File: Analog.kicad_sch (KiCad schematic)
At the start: 0 parts

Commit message: working on audio dac
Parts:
- added U3: MAX98357A, Package_DFN_QFN:TQFN-16-1EP_3x3mm_P0.5mm_EP1.23x1.23mm, symbol Audio:MAX98357A
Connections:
- new net +3V3: U3.7 (VDD), U3.8 (VDD)
- new net GND: U3.11 (GND), U3.15 (GND), U3.17 (PAD), U3.3 (GND)
- new net I2S3_CK: U3.16 (BCLK)
- new net I2S3_SD: U3.1 (DIN)
- new net I2S3_WS: U3.14 (LRCLK)

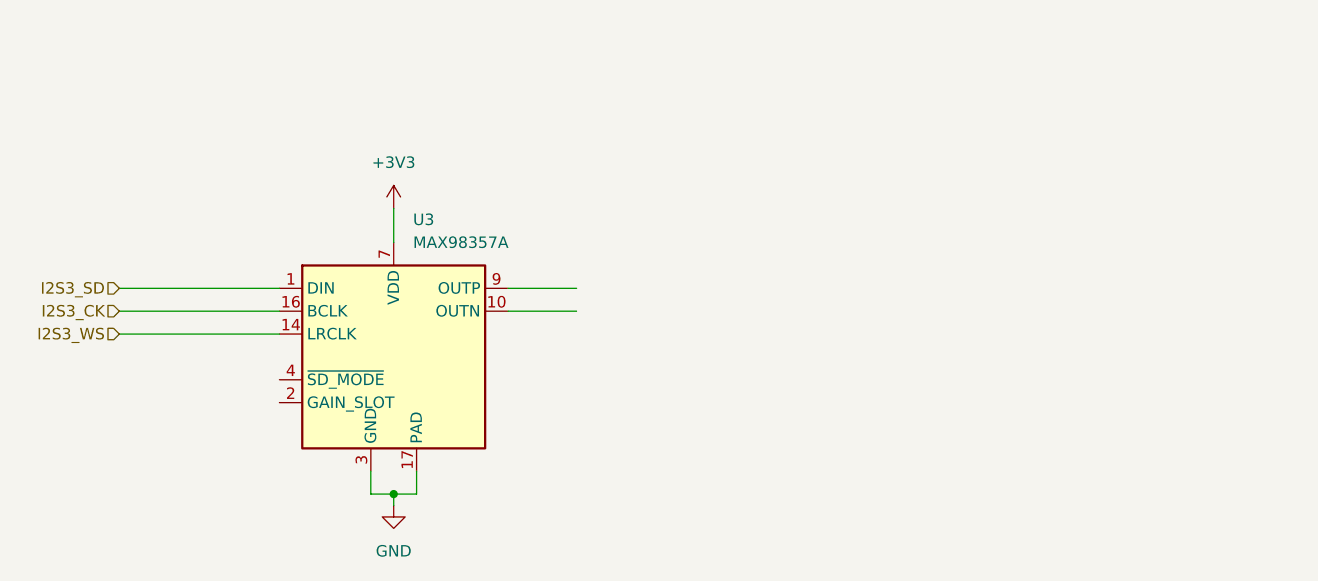
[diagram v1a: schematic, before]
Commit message: audio  dac added
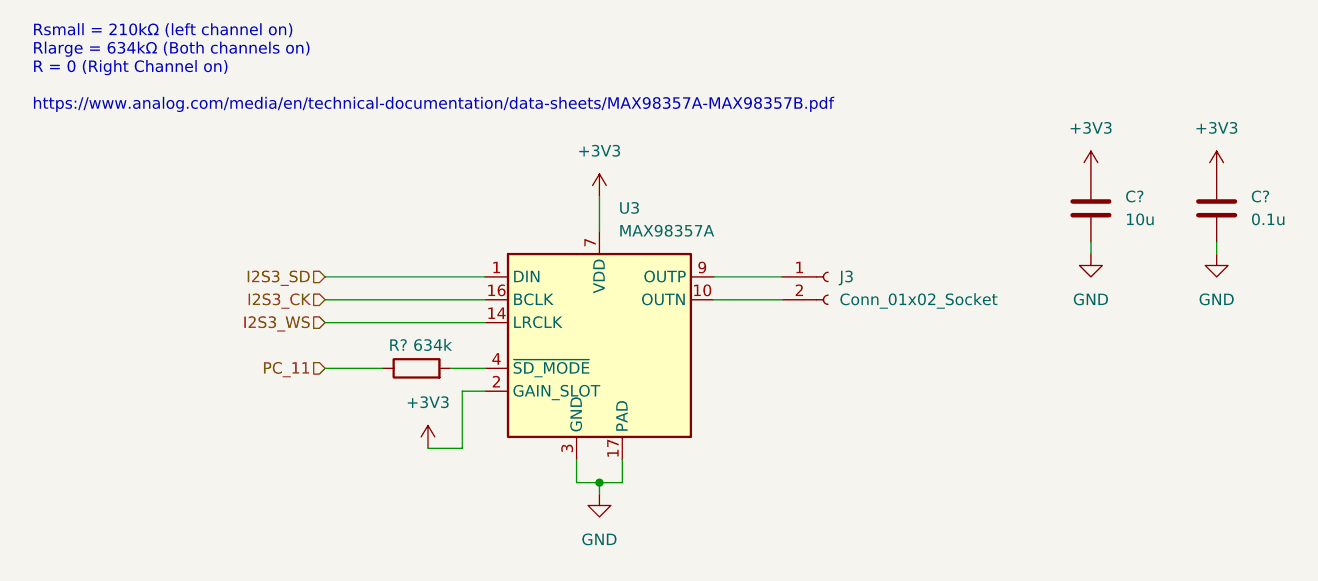
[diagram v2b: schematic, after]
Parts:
- added C?: 0.1u, Capacitor_SMD:C_0603_1608Metric, symbol Device:C
- added C?: 10u, Capacitor_SMD:C_0603_1608Metric, symbol Device:C
- added J3: Conn_01x02_Socket, symbol Connector:Conn_01x02_Socket
- added R?: 634k, Package_DFN_QFN:TQFN-16-1EP_3x3mm_P0.5mm_EP1.23x1.23mm, symbol Device:R
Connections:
- net +3V3: now also U3.2 (GAIN_SLOT), C?.1, C?.1
- net GND: now also C?.2, C?.2
- net at U3.10 (OUTN): now also J3.2 (Pin_2)
- net at U3.4 (~{SD_MODE}): now also R?.2
- net at U3.9 (OUTP): now also J3.1 (Pin_1)
- new net PC_11: R?.1
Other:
- note added: "Rsmall = 210kΩ (left channel on) Rlarge = 634kΩ (Both channels on) R = 0 (Right Channel on) https://www.analog.com/media/en/technical-documentation/data-sheets/MAX98357A-MAX98357B.pdf"
- moved on the sheet: U3

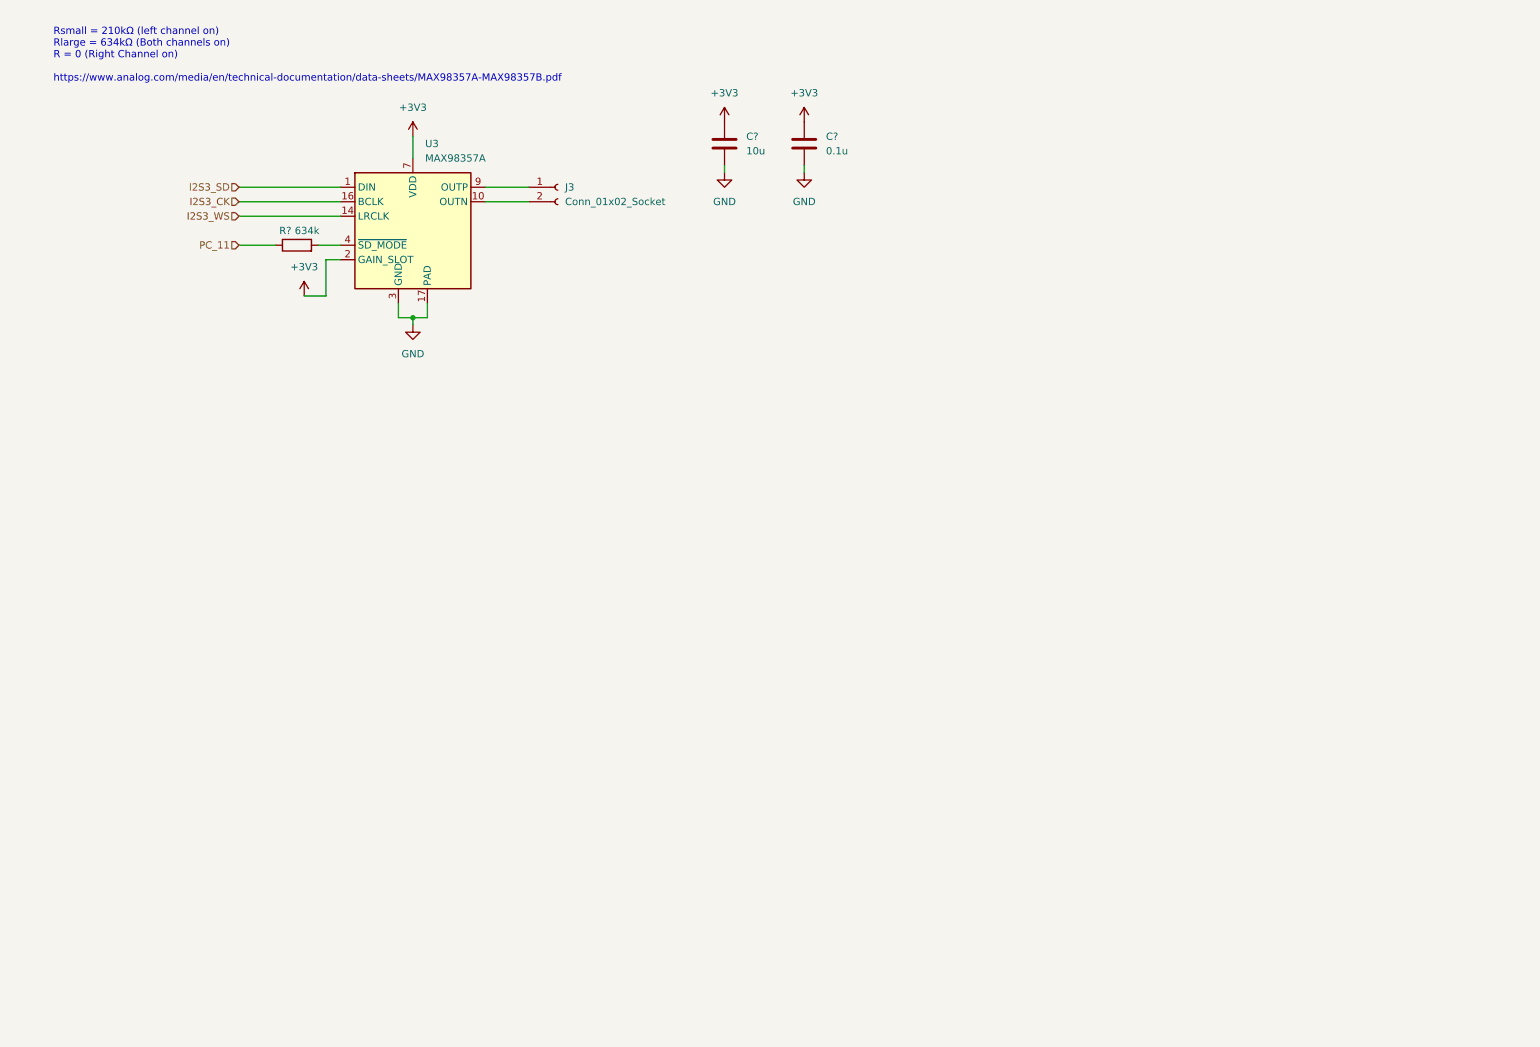
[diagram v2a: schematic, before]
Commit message: fixing audio dac, moving audio to analog section
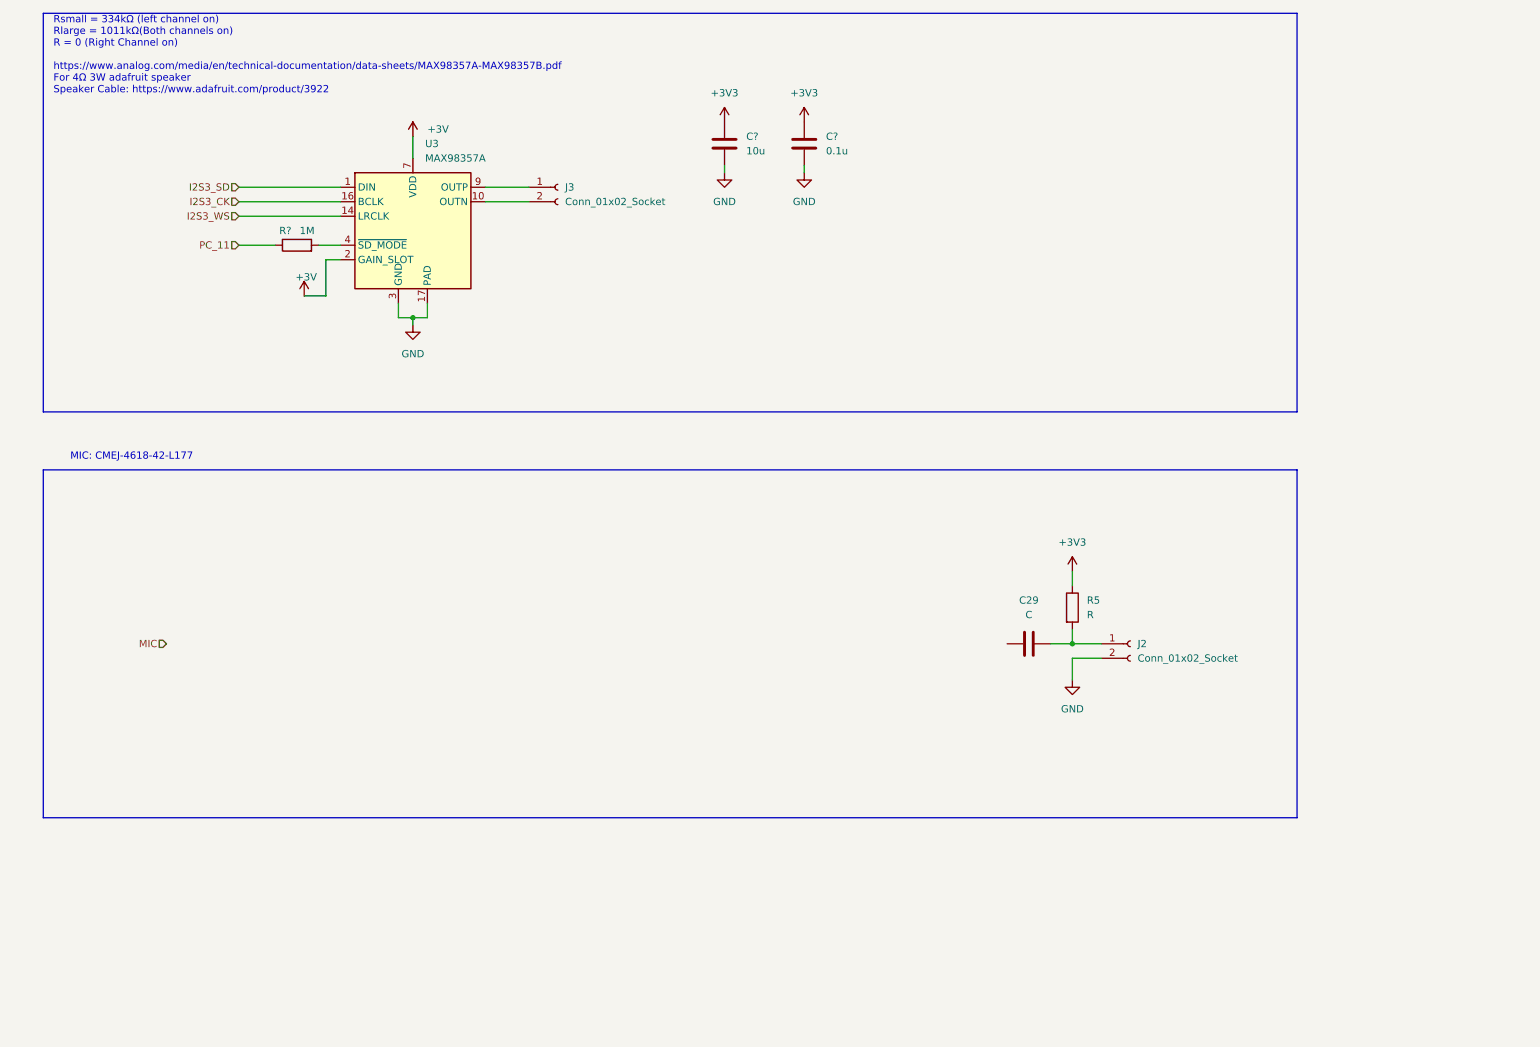
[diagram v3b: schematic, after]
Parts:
- added C29: C, symbol Device:C
- added J2: Conn_01x02_Socket, Package_SO:HTSSOP-20-1EP_4.4x6.5mm_P0.65mm_EP3.4x6.5mm_ThermalVias, symbol Connector:Conn_01x02_Socket
- added R5: R, symbol Device:R
- R?: value 634k -> 1M
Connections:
- net +3V3: now also R5.1; no longer U3.2 (GAIN_SLOT), U3.7 (VDD), U3.8 (VDD)
- net GND: now also J2.2 (Pin_2)
- new net: C29.2, J2.1 (Pin_1), R5.2
- new net +3V: U3.2 (GAIN_SLOT), U3.7 (VDD), U3.8 (VDD)
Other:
- note added: "MIC: CMEJ-4618-42-L177"
- note added: "Rsmall = 334kΩ (left channel on) Rlarge = 1011kΩ(Both channels on) R = 0 (Right Channel on) https://www.analog.com/media/en/technical-documentation/data-sheets/MAX98357A-MAX98357B.pdf For 4Ω 3W adafruit speaker Speaker Cable: https://www.adafruit.com/product/3922"
- note removed: "Rsmall = 210kΩ (left channel on) Rlarge = 634kΩ (Both channels on) R = 0 (Right Channel on) https://www.analog.com/media/en/technical-documentation/data-sheets/MAX98357A-MAX98357B.pdf"

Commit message: op amps
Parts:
- added R25: 50k, symbol Device:R
- added R26: 1k, symbol Device:R
- added R?: 1k, Package_TO_SOT_SMD:SOT-353_SC-70-5, symbol Device:R
- added U4: TLV172IDCK, Package_TO_SOT_SMD:SOT-353_SC-70-5, symbol Amplifier_Operational:TLV172IDCK
- C29: value C -> 1uF
- R5: value R -> 2.2k
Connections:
- net +3V3: now also U4.5 (V+)
- net GND: now also J2.1 (Pin_1), R26.1, U4.2 (V-); no longer J2.2 (Pin_2)
- net MIC: now also R25.2, U4.4
- net at C29.2, R5.2: now also J2.2 (Pin_2); no longer J2.1 (Pin_1)
- net at C29.1: now also R?.1
- new net: R?.2, U4.1 (+)
- new net: R25.1, R26.2, U4.3 (-)
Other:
- note added: "Gain of 1+50"
- note added: "MIC: Adafruit Electret Microphone - 20Hz-20KHz Omnidirectional"
- note removed: "MIC: CMEJ-4618-42-L177"
- moved on the sheet: C29, R5

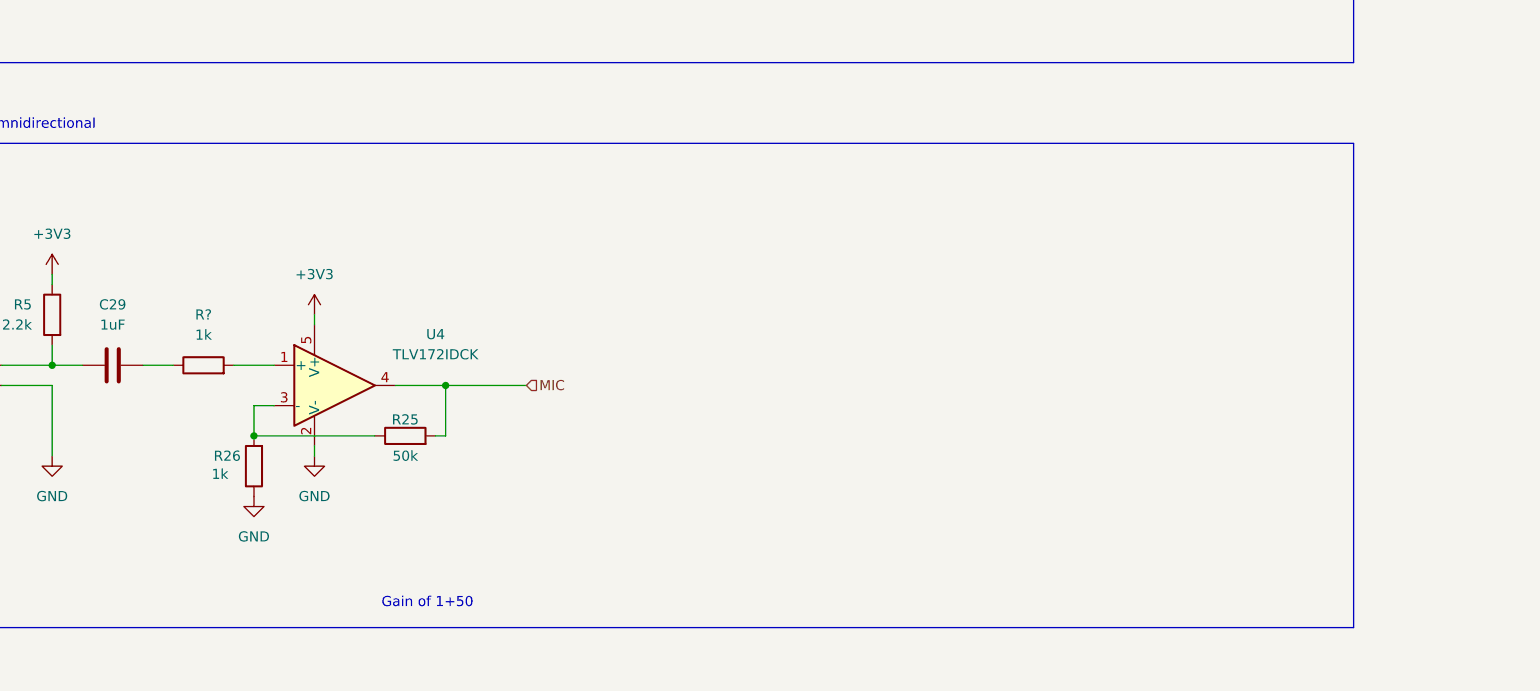
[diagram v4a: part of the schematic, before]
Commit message: added RTC
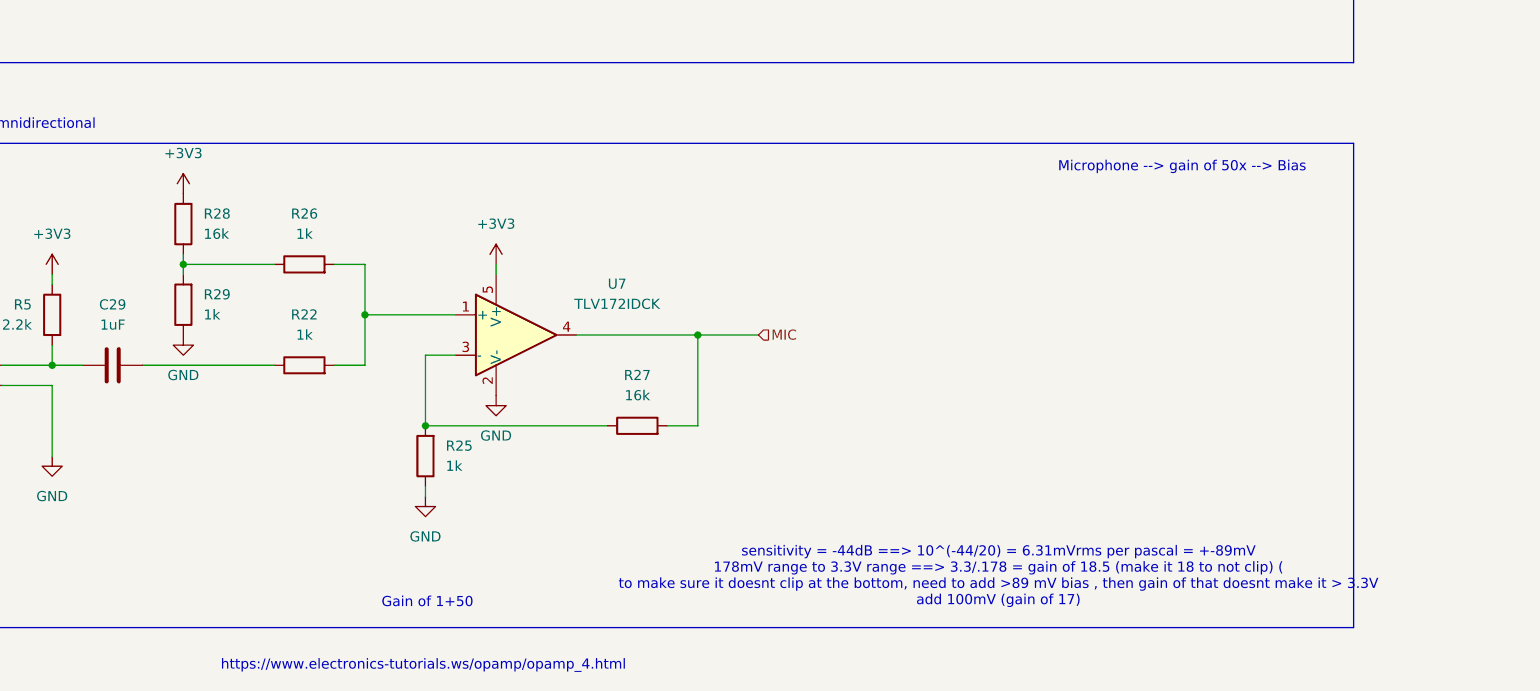
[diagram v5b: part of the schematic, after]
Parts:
- removed R?: 1k, Package_TO_SOT_SMD:SOT-353_SC-70-5, symbol Device:R
- removed U4: TLV172IDCK, Package_TO_SOT_SMD:SOT-353_SC-70-5, symbol Amplifier_Operational:TLV172IDCK
- added R22, R29: 1k, Resistor_SMD:R_0603_1608Metric, symbol Device:R
- added R27, R28: 16k, Resistor_SMD:R_0603_1608Metric, symbol Device:R
- added U7: TLV172IDCK, Package_TO_SOT_SMD:SOT-353_SC-70-5, symbol Amplifier_Operational:TLV172IDCK
- C29: footprint (none) -> Capacitor_SMD:C_0603_1608Metric
- R25: value 50k -> 1k; footprint (none) -> Resistor_SMD:R_0603_1608Metric
- R26, R5: footprint (none) -> Resistor_SMD:R_0603_1608Metric
- R?: footprint Package_DFN_QFN:TQFN-16-1EP_3x3mm_P0.5mm_EP1.23x1.23mm -> Resistor_SMD:R_0603_1608Metric
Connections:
- net +3V3: now also R28.2, U7.5 (V+)
- net GND: now also R25.1, R29.1, U7.2 (V-); no longer R26.1
- net MIC: now also R27.2, U7.4; no longer R25.2
- net at C29.1: now also R22.1
- net at R26.2: now also R22.2, U7.1 (+); no longer R25.1
- new net: R26.1, R28.1, R29.2
- new net: R25.2, R27.1, U7.3 (-)
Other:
- note added: "Microphone --> gain of 50x --> Bias"
- note added: "https://www.electronics-tutorials.ws/opamp/opamp_4.html"
- note added: "sensitivity = -44dB ==> 10^(-44/20) = 6.31mVrms per pascal = +-89mV 178mV range to 3.3V range ==> 3.3/.178 = gain of 18.5 (make it 18 to not clip) ( to make sure it doesnt clip at the bottom, need to add >89 mV bias , then gain of that doesnt make it > 3.3V add 100mV (gain of 17)"
